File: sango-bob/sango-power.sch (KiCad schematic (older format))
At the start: 13 parts, among them P1 CONN_2, P11 1PIN_TH, P12 1PIN_TH, P13 1PIN_TH, P14 1PIN_TH, U1 7805, U4 1117

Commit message: Sango-bc printer controller version 0.1
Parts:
- added R401, R402: 0R, symbol R
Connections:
- net +12P: now also R401.1; no longer C3.1, U1.VI
- net GND: now also R402.2; no longer C9.2, P1.2 (PM)
- new net +12V: C3.1, R401.2, U1.VI
- new net GNDPWR: C9.2, P1.2 (PM), R402.1
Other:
- moved on the sheet: C18, C3, C4, U1, U4

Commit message: Sango-bc v0.2
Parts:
- removed P11, P12, P13, P14: 1PIN_TH, symbol 1PIN_TH
- added H501, H502, H503, H504: HOLE_RMC, symbol HOLE_RMC
- added P506: PWR_12V, symbol CONN_4
- P501: renamed from P1; value CONN_2 -> PWR_12V
- renumbered C3 to C501, C4 to C502, C18 to C503, C9 to C504, D1 to D501, R401 to R501, R402 to R502, R7 to R503, U1 to U501, U4 to U502
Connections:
- net +12P: now also P506.3 (P3), P506.4 (P4)
- net GNDPWR: now also P506.1 (P1), P506.2 (P2)
- net VDD renamed VCC
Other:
- note added: "3.3V 0.8A max"
- note added: "5V 1A max"
- note added: "Could power 5V from USB"
- note added: "Mounting holes"
- note added: "Power LED"
- note added: "Use thick trace for +12P, GNDPWR\nConnect nets with wire or solder bridge"
- moved on the sheet: C501, C502, C503, C504, D501, P501, R501, R502, R503, U501, U502

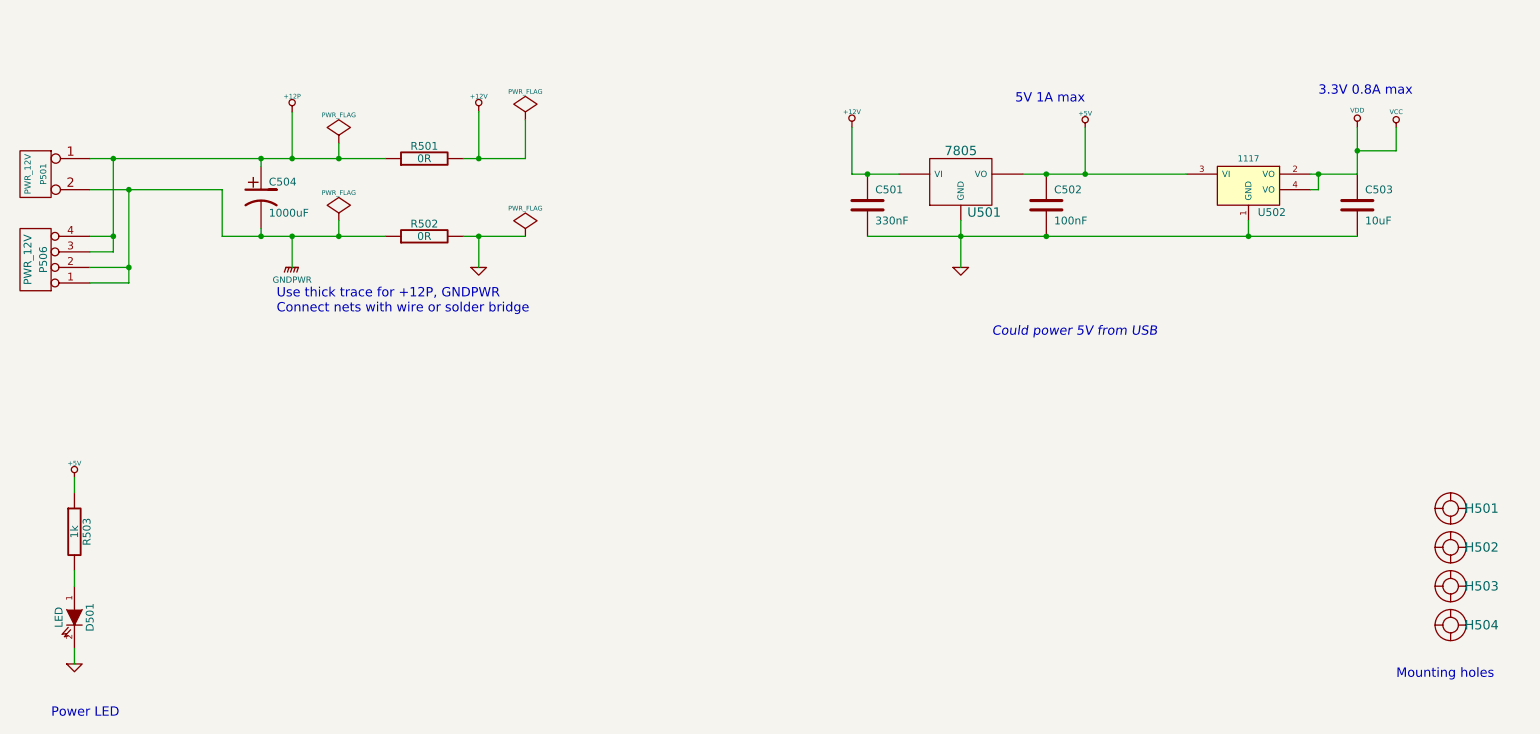
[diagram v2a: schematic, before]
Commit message: Updates to symbols and fix some ERC errors
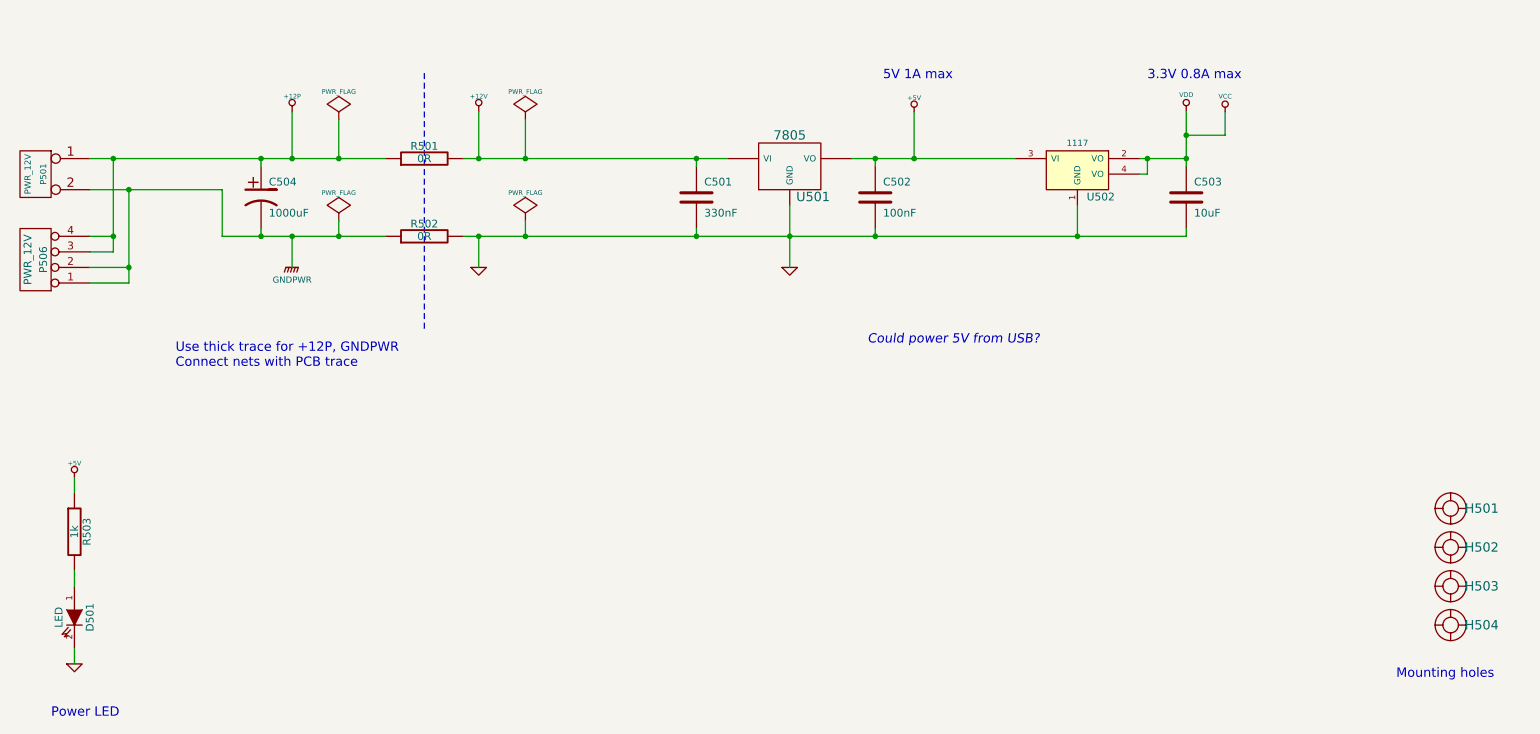
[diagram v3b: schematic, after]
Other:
- note added: "Could power 5V from USB?"
- note added: "Use thick trace for +12P, GNDPWR\nConnect nets with PCB trace"
- note removed: "Could power 5V from USB"
- note removed: "Use thick trace for +12P, GNDPWR\nConnect nets with wire or solder bridge"
- moved on the sheet: C501, C502, C503, U501, U502
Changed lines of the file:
@@
-EESchema Schematic File Version 2  date 03/01/2013 13:12:05
+EESchema Schematic File Version 2  date 22/01/2013 21:21:55
 LIBS:power
 LIBS:device
@@
 Sheet 5 9
 Title "Sango-bc"
-Date "2 jan 2013"
+Date "22 jan 2013"
 Rev "0.2"
 Comp ""
@@
 Comment4 ""
 $EndDescr
+Wire Notes Line
+	3450 1050 3450 2700
+Wire Wire Line
+	8350 2100 8350 2050
+Wire Wire Line
+	6350 1600 6350 1650
+Wire Wire Line
+	5800 1900 5800 2300
+Connection ~ 5200 2100
+Wire Wire Line
+	5200 2100 5200 2050
+Connection ~ 4100 1600
+Wire Wire Line
+	5400 1600 3700 1600
+Connection ~ 1550 2300
+Wire Wire Line
+	1550 2400 1300 2400
+Wire Wire Line
+	1550 2400 1550 1800
+Connection ~ 1450 2100
+Wire Wire Line
+	1450 1600 1450 2200
+Wire Wire Line
+	1450 2200 1300 2200
+Connection ~ 3800 2100
+Wire Wire Line
+	1300 1800 2150 1800
+Connection ~ 2400 2100
+Wire Wire Line
+	2400 2100 2400 2050
+Connection ~ 2900 1600
+Connection ~ 3800 1600
+Wire Wire Line
+	4100 1600 4100 1350
+Connection ~ 2600 1600
+Wire Wire Line
+	2900 1350 2900 1600
+Connection ~ 8100 1600
+Wire Wire Line
+	8100 1700 8100 1600
+Wire Wire Line
+	8100 1700 8050 1700
+Connection ~ 6600 1600
+Wire Wire Line
+	1200 4350 1200 4250
+Wire Wire Line
+	2600 2100 2600 2300
+Wire Wire Line
+	2600 1600 2600 1300
+Wire Wire Line
+	6600 1300 6600 1600
+Connection ~ 5800 2100
+Connection ~ 6350 2100
+Wire Wire Line
+	1200 4850 1200 4750
+Wire Wire Line
+	1200 3750 1200 3650
+Wire Wire Line
+	7250 1600 6200 1600
+Connection ~ 6350 1600
+Connection ~ 5200 1600
+Wire Wire Line
+	8050 1600 8350 1600
+Connection ~ 7650 2100
+Wire Wire Line
+	3800 2100 3800 2300
+Wire Wire Line
+	3800 1300 3800 1600
+Wire Wire Line
+	8350 1450 8600 1450
+Wire Wire Line
+	8600 1450 8600 1300
+Connection ~ 8350 1450
+Wire Wire Line
+	2900 2000 2900 2100
+Connection ~ 2600 2100
+Connection ~ 2900 2100
+Wire Wire Line
+	3200 2100 2150 2100
+Wire Wire Line
+	2150 2100 2150 1800
+Wire Wire Line
+	2400 1600 2400 1650
+Connection ~ 2400 1600
+Wire Wire Line
+	3200 1600 1300 1600
+Wire Wire Line
+	1300 2100 1450 2100
+Connection ~ 1450 1600
+Wire Wire Line
+	1300 2300 1550 2300
+Connection ~ 1550 1800
+Wire Wire Line
+	4100 2100 4100 2000
+Wire Wire Line
+	3700 2100 8350 2100
+Connection ~ 4100 2100
+Wire Wire Line
+	5200 1650 5200 1600
+Wire Wire Line
+	6350 2100 6350 2050
+Wire Wire Line
+	7650 1900 7650 2100
+Wire Wire Line
+	8350 1650 8350 1300
+Connection ~ 8350 1600
 $Comp
 L HOLE_RMC H504
@@
 	1    0    0    -1
 $EndComp
-Text Notes 7100 2750 0    60   Italic 0
-Could power 5V from USB
-Connection ~ 1550 2300
-Wire Wire Line
-	1300 2400 1550 2400
-Wire Wire Line
-	1550 2400 1550 1800
-Connection ~ 1450 2100
-Wire Wire Line
-	1450 1600 1450 2200
-Wire Wire Line
-	1450 2200 1300 2200
-Connection ~ 3800 2100
-Wire Wire Line
-	4100 2100 3700 2100
-Wire Wire Line
-	1300 1800 2150 1800
-Connection ~ 2400 2100
-Wire Wire Line
-	2400 2100 2400 2050
-Connection ~ 2900 1600
-Connection ~ 3800 1600
-Wire Wire Line
-	4100 1350 4100 1600
-Connection ~ 2600 1600
-Wire Wire Line
-	2900 1600 2900 1500
-Connection ~ 9200 1700
-Wire Wire Line
-	9200 1700 9200 1800
-Wire Wire Line
-	9200 1800 9150 1800
-Connection ~ 7700 1700
-Wire Wire Line
-	1200 4350 1200 4250
-Wire Wire Line
-	6900 2300 6900 2000
-Wire Wire Line
-	2600 2100 2600 2300
-Wire Wire Line
-	2600 1600 2600 1300
-Wire Wire Line
-	6200 1400 6200 1700
-Wire Wire Line
-	7700 1700 7700 1400
-Connection ~ 6900 2100
-Wire Wire Line
-	8750 2100 8750 2000
-Connection ~ 7450 2100
-Wire Wire Line
-	9450 1400 9450 1700
-Wire Wire Line
-	1200 4850 1200 4750
-Wire Wire Line
-	1200 3750 1200 3650
-Wire Wire Line
-	7300 1700 8350 1700
-Connection ~ 7450 1700
-Wire Wire Line
-	6200 1700 6500 1700
-Connection ~ 6300 1700
-Wire Wire Line
-	9450 1700 9150 1700
-Wire Wire Line
-	6300 2100 9450 2100
-Connection ~ 8750 2100
-Wire Wire Line
-	3800 2100 3800 2300
-Wire Wire Line
-	4100 1600 3700 1600
-Wire Wire Line
-	3800 1300 3800 1600
-Wire Wire Line
-	9450 1550 9700 1550
-Wire Wire Line
-	9700 1550 9700 1400
-Connection ~ 9450 1550
-Wire Wire Line
-	2900 2000 2900 2100
-Connection ~ 2600 2100
-Connection ~ 2900 2100
-Wire Wire Line
-	3200 2100 2150 2100
-Wire Wire Line
-	2150 2100 2150 1800
-Wire Wire Line
-	2400 1650 2400 1600
-Connection ~ 2400 1600
-Wire Wire Line
-	1300 1600 3200 1600
-Wire Wire Line
-	1450 2100 1300 2100
-Connection ~ 1450 1600
-Wire Wire Line
-	1550 2300 1300 2300
-Connection ~ 1550 1800
+Text Notes 6300 2800 0    60   Italic 0
+Could power 5V from USB?
 $Comp
 L CONN_4 P506
@@
 $EndComp
 $Comp
-L PWR_FLAG #FLG065
+L PWR_FLAG #FLG066
 U 1 1 50E0735A
-P 4100 2100
-F 0 "#FLG065" H 4100 2195 30  0001 C CNN
-F 1 "PWR_FLAG" H 4100 2280 30  0000 C CNN
-	1    4100 2100
+P 4100 2000
+F 0 "#FLG066" H 4100 2095 30  0001 C CNN
+F 1 "PWR_FLAG" H 4100 2180 30  0000 C CNN
+	1    4100 2000
 	1    0    0    -1
 $EndComp
@@
 Text Notes 9700 4950 0    60   ~ 0
 Mounting holes
-Text Notes 9200 1200 0    60   ~ 0
+Text Notes 8100 1100 0    60   ~ 0
 3.3V 0.8A max
-Text Notes 7250 1250 0    60   ~ 0
+Text Notes 6400 1100 0    60   ~ 0
 5V 1A max
-Text Notes 2500 2600 0    60   ~ 0
-Use thick trace for +12P, GNDPWR\nConnect nets with wire or solder bridge
-$Comp
-L PWR_FLAG #FLG066
+Text Notes 1850 2950 0    60   ~ 0
+Use thick trace for +12P, GNDPWR\nConnect nets with PCB trace
+$Comp
+L PWR_FLAG #FLG067
 U 1 1 50D59DDD
 P 4100 1350
-F 0 "#FLG066" H 4100 1445 30  0001 C CNN
+F 0 "#FLG067" H 4100 1445 30  0001 C CNN
 F 1 "PWR_FLAG" H 4100 1530 30  0000 C CNN
 	1    4100 1350
@@
 $EndComp
 $Comp
-L PWR_FLAG #FLG067
+L PWR_FLAG #FLG068
 U 1 1 50D59DDB
 P 2900 2000
-F 0 "#FLG067" H 2900 2095 30  0001 C CNN
+F 0 "#FLG068" H 2900 2095 30  0001 C CNN
 F 1 "PWR_FLAG" H 2900 2180 30  0000 C CNN
 	1    2900 2000
@@
 $EndComp
 $Comp
-L VCC #PWR068
+L VCC #PWR069
 U 1 1 50D58C15
-P 9700 1400
-F 0 "#PWR068" H 9700 1500 30  0001 C CNN
-F 1 "VCC" H 9700 1500 30  0000 C CNN
-	1    9700 1400
-	1    0    0    -1
-$EndComp
-$Comp
-L +12V #PWR069
-U 1 1 5065AC4A
-P 6200 1400
-F 0 "#PWR069" H 6200 1350 20  0001 C CNN
-F 1 "+12V" H 6200 1500 30  0000 C CNN
-	1    6200 1400
+P 8600 1300
+F 0 "#PWR069" H 8600 1400 30  0001 C CNN
+F 1 "VCC" H 8600 1400 30  0000 C CNN
+	1    8600 1300
 	1    0    0    -1
 $EndComp
@@
 L C C503
 U 1 1 504D1B3E
-P 9450 1900
-F 0 "C503" H 9500 2000 50  0000 L CNN
-F 1 "10uF" H 9500 1800 50  0000 L CNN
-	1    9450 1900
+P 8350 1850
+F 0 "C503" H 8400 1950 50  0000 L CNN
+F 1 "10uF" H 8400 1750 50  0000 L CNN
+	1    8350 1850
 	1    0    0    -1
 $EndComp
@@
 L VDD #PWR073
 U 1 1 504A2506
-P 9450 1400
-F 0 "#PWR073" H 9450 1500 30  0001 C CNN
-F 1 "VDD" H 9450 1510 30  0000 C CNN
-	1    9450 1400
+P 8350 1300
+F 0 "#PWR073" H 8350 1400 30  0001 C CNN
+F 1 "VDD" H 8350 1410 30  0000 C CNN
+	1    8350 1300
 	1    0    0    -1
 $EndComp
@@
 L PWR_FLAG #FLG076
 U 1 1 5047CFEE
-P 2900 1500
-F 0 "#FLG076" H 2900 1595 30  0001 C CNN
-F 1 "PWR_FLAG" H 2900 1680 30  0000 C CNN
-	1    2900 1500
+P 2900 1350
+F 0 "#FLG076" H 2900 1445 30  0001 C CNN
+F 1 "PWR_FLAG" H 2900 1530 30  0000 C CNN
+	1    2900 1350
 	1    0    0    -1
 $EndComp
@@
 L 1117 U502
 U 1 1 5047CFB9
-P 8750 1750
-F 0 "U502" H 8900 1554 50  0000 C CNN
-F 1 "1117" H 8750 1900 40  0000 C CNN
-	1    8750 1750
+P 7650 1650
+F 0 "U502" H 7800 1454 50  0000 C CNN
+F 1 "1117" H 7650 1800 40  0000 C CNN
+	1    7650 1650
 	1    0    0    -1
 $EndComp
@@
 L +5V #PWR077
 U 1 1 5047CCAB
-P 7700 1400
-F 0 "#PWR077" H 7700 1490 20  0001 C CNN
-F 1 "+5V" H 7700 1490 30  0000 C CNN
-	1    7700 1400
+P 6600 1300
+F 0 "#PWR077" H 6600 1390 20  0001 C CNN
+F 1 "+5V" H 6600 1390 30  0000 C CNN
+	1    6600 1300
 	1    0    0    -1
 $EndComp
@@
 L GND #PWR078
 U 1 1 5047CCA3
-P 6900 2300
-F 0 "#PWR078" H 6900 2300 30  0001 C CNN
-F 1 "GND" H 6900 2230 30  0001 C CNN
-	1    6900 2300
+P 5800 2300
+F 0 "#PWR078" H 5800 2300 30  0001 C CNN
+F 1 "GND" H 5800 2230 30  0001 C CNN
+	1    5800 2300
 	1    0    0    -1
 $EndComp
@@
 L C C502
 U 1 1 5047CC9A
-P 7450 1900
-F 0 "C502" H 7500 2000 50  0000 L CNN
-F 1 "100nF" H 7500 1800 50  0000 L CNN
-	1    7450 1900
+P 6350 1850
+F 0 "C502" H 6400 1950 50  0000 L CNN
+F 1 "100nF" H 6400 1750 50  0000 L CNN
+	1    6350 1850
 	1    0    0    -1
 $EndComp
@@
 L C C501
 U 1 1 5047CC95
-P 6300 1900
-F 0 "C501" H 6350 2000 50  0000 L CNN
-F 1 "330nF" H 6350 1800 50  0000 L CNN
-	1    6300 1900
+P 5200 1850
+F 0 "C501" H 5250 1950 50  0000 L CNN
+F 1 "330nF" H 5250 1750 50  0000 L CNN
+	1    5200 1850
 	1    0    0    -1
 $EndComp
@@
 L 7805 U501
 U 1 1 5047CC85
-P 6900 1750
-F 0 "U501" H 7050 1554 60  0000 C CNN
-F 1 "7805" H 6900 1950 60  0000 C CNN
-	1    6900 1750
-	1    0    0    -1
-$EndComp
+P 5800 1650
+F 0 "U501" H 5950 1454 60  0000 C CNN
+F 1 "7805" H 5800 1850 60  0000 C CNN
+	1    5800 1650
+	1    0    0    -1
+$EndComp
